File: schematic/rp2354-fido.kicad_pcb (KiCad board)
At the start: 2 copper layers, 18 x 37.5 mm, 36 parts, among them J1 USB_C_Receptacle_USB2.0_14P, SW1 SW_Push, U1 RP2354A, U2 AP2112K-3.3, U3 USBLC6-2SC6, Y1 Crystal_Small

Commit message: add code, finalize pcb
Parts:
- moved R2 24.7 mm to (94.9, 79.6), turned to -90 degrees
- moved R7 23.2 mm to (127.2, 77.2), turned to 0 degrees
- moved J1 22.0 mm to (127.5, 83.8), turned to 90 degrees
- moved R1 21.9 mm to (98.8, 90.2), turned to -90 degrees
- moved SW1 21.5 mm to (98.2, 76.7), turned to 180 degrees
- moved Y1 21.4 mm to (96.9, 83.7), turned to 90 degrees
- moved C16 19.4 mm to (98.8, 79.7), turned to 90 degrees
- moved R8 19.3 mm to (124.2, 77.2), turned to 0 degrees
- moved C7 18.5 mm to (101.2, 90.7), turned to 90 degrees
- moved C17 17.8 mm to (100.2, 88.2), turned to 180 degrees
- moved R9 16.7 mm to (100.2, 82.2), turned to -90 degrees
- moved C8 16.0 mm to (102.8, 89.7), turned to 180 degrees
- moved C5 14.7 mm to (102.9, 88.2), turned to 0 degrees
- moved C1 13.8 mm to (104.8, 76.7), turned to 90 degrees
- moved TP2 13.7 mm to (120.2, 78.2), turned to 0 degrees
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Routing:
- net GND: track 11.9 -> 130.2 mm, vias 3 -> 15
- net +3V3: track 35.3 -> 88.0 mm, vias 0 -> 12
- net +1V1: track 7.56 -> 25.8 mm
- net Net-(U1-GPIO16): track 5.47 -> 17.3 mm, vias 0 -> 2
- net Net-(U1-RUN): track 0.00 -> 8.39 mm, vias 0 -> 2
- net Net-(U1-VREG_LX): track 4.44 -> 5.06 mm
- added copper zone on B.Cu, net GND
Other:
- board size 18 x 37.5 mm -> 37.5 x 18 mm
- board text added: "RP2354 FIDO2 KEY v1"
- board text added: "pls work"

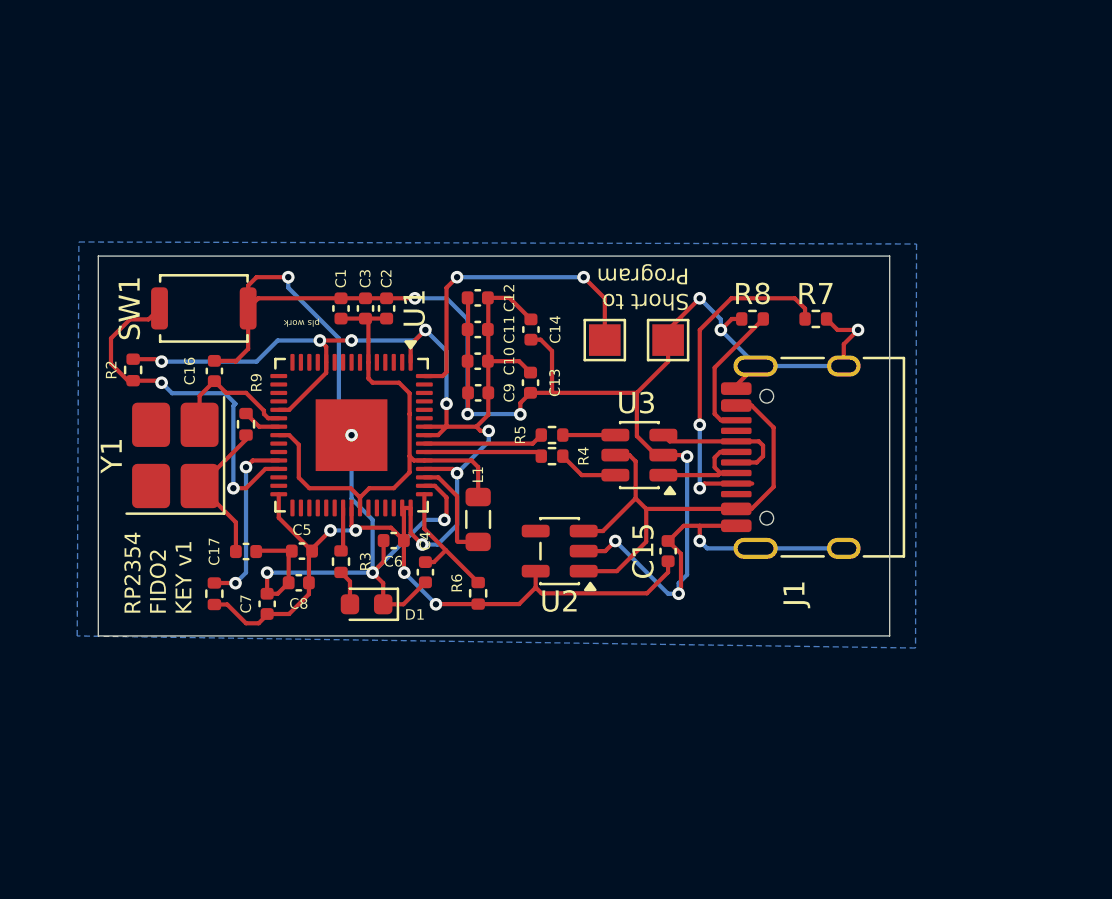
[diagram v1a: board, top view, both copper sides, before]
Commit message: added debug pins, minor layout changes
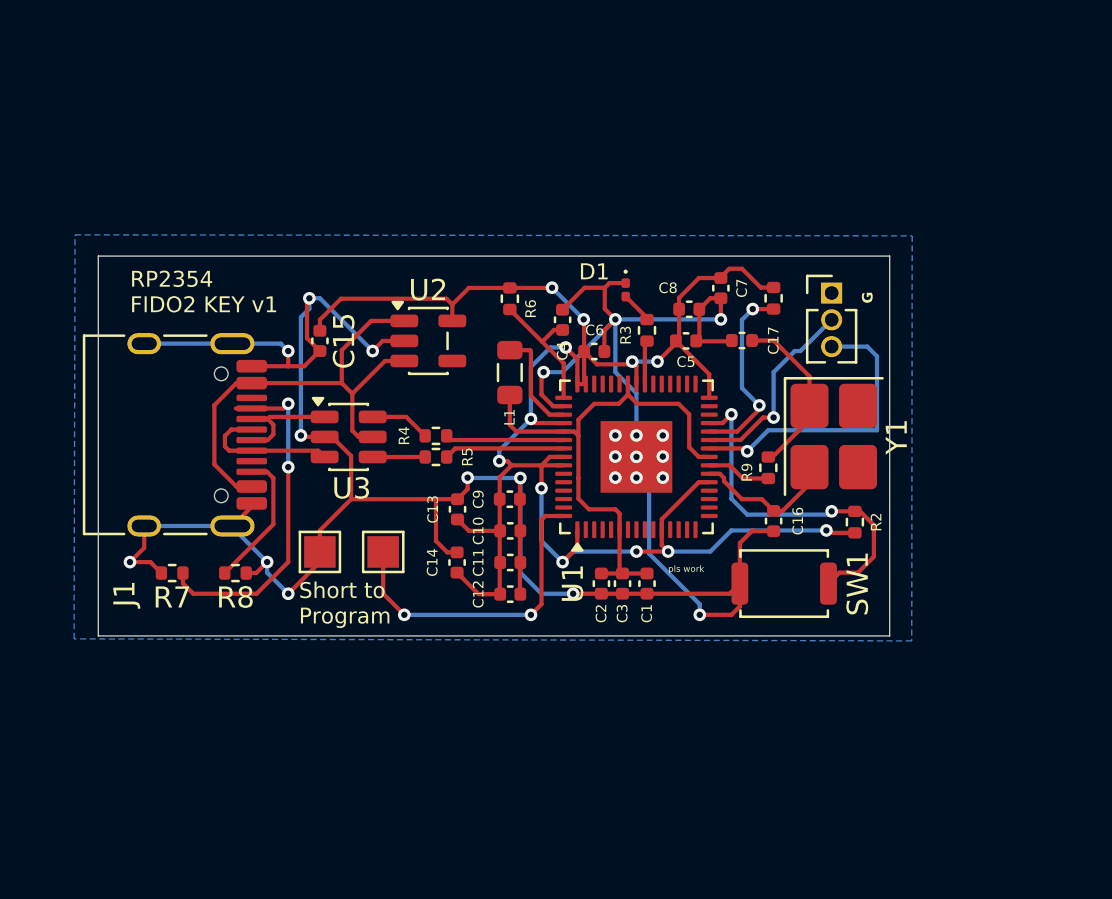
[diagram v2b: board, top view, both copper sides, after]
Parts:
- added J2: Conn_01x03_Pin, Connector_PinHeader_1.27mm:PinHeader_1x03_P1.27mm_Vertical, F.Cu at (128.0, 76.0)
- D1: footprint LED_SMD:LED_0603_1608Metric -> LED_SMD:LED_0201_0603Metric
- moved R2 35.0 mm to (129.1, 86.9), turned to 90 degrees
- moved R7 32.8 mm to (96.8, 89.3), turned to 180 degrees
- moved Y1 31.2 mm to (128.1, 82.8), turned to -90 degrees
- moved J1 31.1 mm to (96.5, 82.7), turned to -90 degrees
- moved SW1 30.4 mm to (125.8, 89.8), turned to 0 degrees
- moved R1 30.0 mm to (125.2, 76.2), turned to 90 degrees
- moved C16 27.4 mm to (125.2, 86.8), turned to -90 degrees
- moved R8 27.3 mm to (99.8, 89.3), turned to 180 degrees
- moved C7 26.2 mm to (122.8, 75.8), turned to -90 degrees
- moved C17 25.5 mm to (123.8, 78.2), turned to 0 degrees
- moved R9 24.8 mm to (125.0, 84.3), turned to 90 degrees
- moved C8 22.6 mm to (121.2, 76.8), turned to 0 degrees
- moved C5 20.7 mm to (121.1, 78.3), turned to 180 degrees
- moved C1 19.5 mm to (119.2, 89.8), turned to -90 degrees
- moved TP2 19.3 mm to (103.8, 88.3), turned to 180 degrees
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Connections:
- U1 pad 24: unconnected-(U1-SWCLK-Pad24) -> Net-(J2-Pin_3)
- U1 pad 25: unconnected-(U1-SWDIO-Pad25) -> Net-(J2-Pin_2)
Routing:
- net Net-(J2-Pin_3): track 0.00 -> 14.3 mm, vias 0 -> 1
- net Net-(J2-Pin_2): track 0.00 -> 9.42 mm, vias 0 -> 1
- net Net-(U1-XOUT): track 1.81 -> 3.06 mm
- net GND: track 130.2 -> 131.3 mm, vias 15 -> 23
- net Net-(C17-Pad2): track 7.14 -> 8.17 mm
- net Net-(U1-RUN): track 8.39 -> 9.14 mm
- net Net-(U1-XIN): track 6.23 -> 6.90 mm
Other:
- board text added: "G"

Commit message: added debug pads, new usb c connector + BOM
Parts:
- J1: footprint Connector_USB:USB_C_Receptacle_HRO_TYPE-C-31-M-12 -> type c:HRO_TYPE-C-31-G-10
- SW1: value SW_Push -> SW_Push_Dual; footprint Button_Switch_SMD:SW_Push_SPST_NO_Alps_SKRK -> Button_Switch_SMD:SW_Push_1P1T_XKB_TS-1187A
- moved C16 6.96 mm to (131.9, 84.8)
- moved R2 6.33 mm to (131.5, 81.0), turned to -90 degrees
- moved SW1 2.47 mm to (128.0, 88.8), turned to 180 degrees
- moved J1 1.31 mm to (95.3, 83.3)
- moved R8 1.01 mm to (100.0, 90.2), turned to 0 degrees
- moved R7 1.01 mm to (97.0, 90.2)
- moved D1 0.56 mm to (118.7, 75.5), turned to 0 degrees
- turned J2 to 90 degrees
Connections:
- J1 pad A4: Net-(U2-EN) -> Net-(J1-VBUS_A)
- J1 pad A6: Net-(J1-D+-PadA6) -> Net-(J1-D+)
- J1 pad A7: Net-(J1-D--PadA7) -> Net-(J1-D-)
- J1 pad B9: Net-(U2-EN) -> Net-(J1-VBUS_A)
- U2 pad 1: Net-(U2-EN) -> Net-(J1-VBUS_A)
- U2 pad 3: Net-(U2-EN) -> Net-(J1-VBUS_A)
- U3 pad 1: Net-(J1-D--PadA7) -> Net-(J1-D-)
- U3 pad 3: Net-(J1-D+-PadA6) -> Net-(J1-D+)
- U3 pad 5: Net-(U2-EN) -> Net-(J1-VBUS_A)
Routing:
- net Net-(U2-EN): track 23.2 -> 0.00 mm
- net Net-(J1-VBUS_A): track 0.00 -> 16.7 mm, vias 0 -> 3
- net Net-(J1-VCONN): track 6.60 -> 17.3 mm, vias 0 -> 2
- net Net-(J1-CC): track 16.4 -> 8.94 mm, vias 2 -> 0
- net Net-(J1-D+-PadA6): track 6.83 -> 0.00 mm
- net Net-(U1-XIN): track 6.90 -> 13.3 mm
- net Net-(J1-D--PadA7): track 5.48 -> 0.00 mm
- net Net-(U1-GPIO16): track 16.9 -> 20.7 mm
- net Net-(J1-D-): track 0.00 -> 3.46 mm
- net Net-(J1-D+): track 0.00 -> 3.07 mm
- net GND: track 131.3 -> 128.7 mm, vias 23 -> 24
- net Net-(J2-Pin_2): track 9.42 -> 11.6 mm
- net +3V3: track 88.0 -> 86.2 mm, vias 12 -> 10
- net Net-(J2-Pin_3): track 14.3 -> 15.1 mm
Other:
- board size 37.5 x 18 mm -> 40.2 x 18 mm

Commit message: added gerber and bom
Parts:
- added FID1: Fiducial, Fiducial:Fiducial_1mm_Mask2mm, F.Cu at (134.0, 90.0)
- added FID2: Fiducial, Fiducial:Fiducial_1mm_Mask2mm, F.Cu at (134.0, 76.8)
- added FID3: Fiducial, Fiducial:Fiducial_1mm_Mask2mm, F.Cu at (97.2, 76.2)
- moved J2 0.54 mm to (128.2, 76.5)
- moved C15 0.34 mm to (104.0, 78.5)
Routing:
- net GND: track 128.7 -> 118.8 mm, vias 24 -> 22
- net +3V3: track 86.2 -> 83.0 mm, vias 10 -> 9
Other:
- board size 40.2 x 18 mm -> 41.8 x 18 mm
- board text added: "FIDO2 key v1"
- board text added: "bootsel"
- board text removed: "RP2354 FIDO2 KEY v1"
- board text removed: "Short to Program"
